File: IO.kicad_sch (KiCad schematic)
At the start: 5 parts, among them J1 BackBone, J2 D1, J3 D2

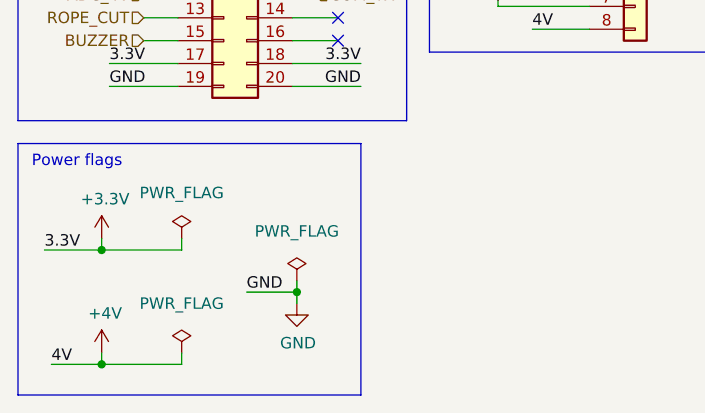
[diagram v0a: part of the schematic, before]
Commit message: V1
- Corrected SD-cards footprint and schematical represantation;
- Corrected RTC shematics:
	- changed oscilators power supply from internal 3v3 to Vbat so RTC works when PCB is disconnected from external power supply [PWR PCB];
	- 32 kHz to microcontroller now comes from RTC module;
	- added 100 nF decoupling capacitor to Vbat RTC pin.
- Corrected couple connections and component placement on PCB
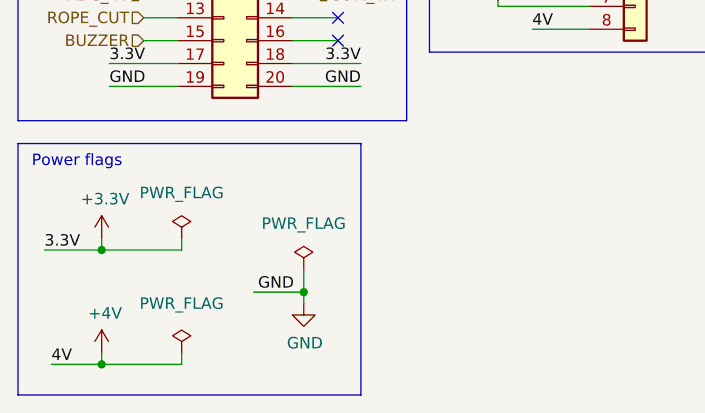
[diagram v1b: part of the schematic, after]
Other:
- company: (none) -> BASEMENT
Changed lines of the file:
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@@
 (kicad_sch (version 20211123) (generator eeschema)
   (paper "A4")
+  (title_block
+    (date "%%date%%")
+    (rev "%%version%%")
+    (company "BASEMENT")
+  )
+  (junction (at 46.99 72.39) (diameter 0) (color 0 0 0 0)
+  )
   (junction (at 24.5364 80.4164) (diameter 0) (color 0 0 0 0)
-  )
-  (junction (at 46.228 72.39) (diameter 0) (color 0 0 0 0)
   )
   (junction (at 24.5364 67.7164) (diameter 0) (color 0 0 0 0)
@@
     (stroke (width 0) (type default) (color 0 0 0 0))
   )
-  (wire (pts (xy 46.228 71.12) (xy 46.228 72.39))
-    (stroke (width 0) (type default) (color 0 0 0 0))
-  )
   (wire (pts (xy 45.72 44.45) (xy 50.8 44.45))
     (stroke (width 0) (type default) (color 0 0 0 0))
@@
     (stroke (width 0) (type default) (color 0 0 0 0))
   )
+  (wire (pts (xy 46.99 69.85) (xy 46.99 72.39))
+    (stroke (width 0) (type default) (color 0 0 0 0))
+  )
   (wire (pts (xy 45.72 29.21) (xy 53.34 29.21))
     (stroke (width 0) (type default) (color 0 0 0 0))
@@
     (stroke (width 0) (type default) (color 0 0 0 0))
   )
-  (wire (pts (xy 46.228 73.66) (xy 46.228 72.39))
+  (wire (pts (xy 46.99 73.66) (xy 46.99 72.39))
     (stroke (width 0) (type default) (color 0 0 0 0))
   )
@@
     (stroke (width 0) (type default) (color 0 0 0 0))
   )
-  (wire (pts (xy 40.64 72.39) (xy 46.228 72.39))
+  (wire (pts (xy 41.402 72.39) (xy 46.99 72.39))
     (stroke (width 0) (type default) (color 0 0 0 0))
   )
@@
     (effects (font (size 1.27 1.27)) (justify left bottom))
   )
-  (label "GND" (at 40.64 72.39 0)
+  (label "GND" (at 41.91 72.39 0)
     (effects (font (size 1.27 1.27)) (justify left bottom))
   )
@@
     (pin "7")
     (pin "8")
-  )
-  (symbol (lib_id "power:PWR_FLAG") (at 46.228 71.12 0) (unit 1)
-    (in_bom yes) (on_board yes) (fields_autoplaced)
-    (property "Reference" "#FLG0101" (id 0) (at 46.228 69.215 0)
-      (effects (font (size 1.27 1.27)) hide)
-    )
-    (property "Value" "PWR_FLAG" (id 1) (at 46.228 65.6336 0))
-    (property "Footprint" "" (id 2) (at 46.228 71.12 0)
-      (effects (font (size 1.27 1.27)) hide)
-    )
-    (property "Datasheet" "~" (id 3) (at 46.228 71.12 0)
-      (effects (font (size 1.27 1.27)) hide)
-    )
-    (pin "1")
   )
   (symbol (lib_id "power:+4V") (at 24.5364 79.1464 0) (unit 1)
@@
     (pin "8")
   )
-  (symbol (lib_id "power:GND") (at 46.228 73.66 0) (unit 1)
+  (symbol (lib_id "power:GND") (at 46.99 73.66 0) (unit 1)
     (in_bom yes) (on_board yes)
-    (property "Reference" "#PWR0103" (id 0) (at 46.228 80.01 0)
-      (effects (font (size 1.27 1.27)) hide)
-    )
-    (property "Value" "GND" (id 1) (at 46.355 78.0542 0))
-    (property "Footprint" "" (id 2) (at 46.228 73.66 0)
-      (effects (font (size 1.27 1.27)) hide)
-    )
-    (property "Datasheet" "" (id 3) (at 46.228 73.66 0)
+    (property "Reference" "#PWR0103" (id 0) (at 46.99 80.01 0)
+      (effects (font (size 1.27 1.27)) hide)
+    )
+    (property "Value" "GND" (id 1) (at 47.117 78.0542 0))
+    (property "Footprint" "" (id 2) (at 46.99 73.66 0)
+      (effects (font (size 1.27 1.27)) hide)
+    )
+    (property "Datasheet" "" (id 3) (at 46.99 73.66 0)
       (effects (font (size 1.27 1.27)) hide)
     )
@@
     )
   )
+  (symbol (lib_id "power:PWR_FLAG") (at 46.99 69.85 0) (unit 1)
+    (in_bom yes) (on_board yes) (fields_autoplaced)
+    (property "Reference" "#FLG0101" (id 0) (at 46.99 67.945 0)
+      (effects (font (size 1.27 1.27)) hide)
+    )
+    (property "Value" "PWR_FLAG" (id 1) (at 46.99 64.77 0))
+    (property "Footprint" "" (id 2) (at 46.99 69.85 0)
+      (effects (font (size 1.27 1.27)) hide)
+    )
+    (property "Datasheet" "~" (id 3) (at 46.99 69.85 0)
+      (effects (font (size 1.27 1.27)) hide)
+    )
+    (pin "1")
+  )
   (symbol (lib_id "power:+BATT") (at 68.58 40.005 0) (unit 1)
